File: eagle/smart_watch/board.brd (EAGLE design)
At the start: 100 x 80 mm, 38 parts, among them U1 MCP73831, U2 TPS61200, U3 MAX1704X, U4 V_REG_LDOSMD

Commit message: V1 of Schema is donepending feedback
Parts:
- removed QG1: SM77H, crystal:SM77H
- removed VIBE: (no value), SparkFun-Connectors:JST-2-PTH-NS
- added LED1, LED2, LED3, LED4: (no value), SparkFun-LED:LED-0603
- added R12, R13, R19, R20: Pullup, SparkFun-Passives:0402-RES
- added R14, R16, R17, R18: 330, SparkFun-Passives:0402-RES
- added R15: 10k, SparkFun-Passives:0402-RES
- added S1: (no value), SparkFun-Electromechanical:JOYSTICK_MINI
- added U$3: MOTOR10MM, SparkFun-Electromechanical:VIBE-MOTOR-10MM
- added Y1: (no value), SparkFun-FreqCtrl:CRYSTAL-SMD-5X3
- C1, C2: value (none) -> 4.7uF
- C12, C13: value 0.1uF -> 16pF; device SparkFun-Capacitors:0402-CAP -> SparkFun-Passives:0402-CAP
- C3, C6: value (none) -> .1uF
- C4: value (none) -> 10uF
- C5: value (none) -> 22uF
- C7: value (none) -> 1uF
- C8: value (none) -> 10nF
- L1: value (none) -> 4.7uH
- R11: value (none) -> 4.7k
- R2, R5, R6: value (none) -> 10k
- R3, R8: value (none) -> 2M
- R4: value (none) -> 100
- R7, R9: value (none) -> 220k
- U$2: value BLUERADIO_BR-C40NINTERNAL -> BLUETOOTH-RN41"; device SparkFun-RF:BLUETOOTH-INTERNAL-FP -> SparkFun-RF:RN41
- moved C13 67.1 mm to (-48.3, -16.5)
- moved C12 66.0 mm to (-48.3, -14.0)
- moved U$2 57.9 mm to (-34.3, -25.4)
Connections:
- new net ACC_INT1: ACCELEROMETER.8, U$1.10
- new net ACC_INT2: ACCELEROMETER.9, U$1.14
- new net JCENTER: S1.CTR, U$1.21
- new net JDOWN: S1.D, U$1.43
- new net JLEFT: S1.C, U$1.48
- new net JRIGHT: S1.B, U$1.18
- new net JUP: S1.A, U$1.37
- new net MISO1: U$1.26, U$2.24
- new net MOSI1: U$1.38, U$2.2
- new net N$12: LED1.A, U$2.21
- new net N$13: LED1.C, R14.2
- new net N$14: LED2.C, R16.2
- new net N$15: LED3.A, U$1.25
- new net N$16: LED4.A, U$1.24
- new net N$17: LED3.C, R17.2
- new net N$18: LED4.C, R18.2
- new net SCK1: U$1.13, U$2.6
- new net SCL: ACCELEROMETER.14, R13.1, R19.1, R20.1, U$1.15, U3.7
- new net SDA: ACCELEROMETER.13, R12.1, U$1.16, U3.8
- new net SSEL1: U$1.2, U$2.23
- new net XTALIN: C13.2, U$1.6, Y1.3
- new net XTALOUT: C12.2, U$1.7, Y1.1
- net 3.3V: now also ACCELEROMETER.7, R12.2, R13.2, R19.2, R20.2, U$2.11
- net GND: now also ACCELEROMETER.12, C12.1, C13.1, R14.1, R15.1, R16.1, R17.1, R18.1, S1.GND, U$3.-; no longer C12.2, C13.2, QG1.2, VIBE.1
- net N$1: now also LED2.A, U$2.19; no longer C13.1, QG1.3, U$1.7
- net N$11: now also R15.2, U$2.22; no longer C12.1, QG1.4, U$1.6
- net SCRX: now also U$1.46
- net SCTX: now also U$1.47
- net VIBE_PWM: now also U$1.20, U$3.+; no longer VIBE.2

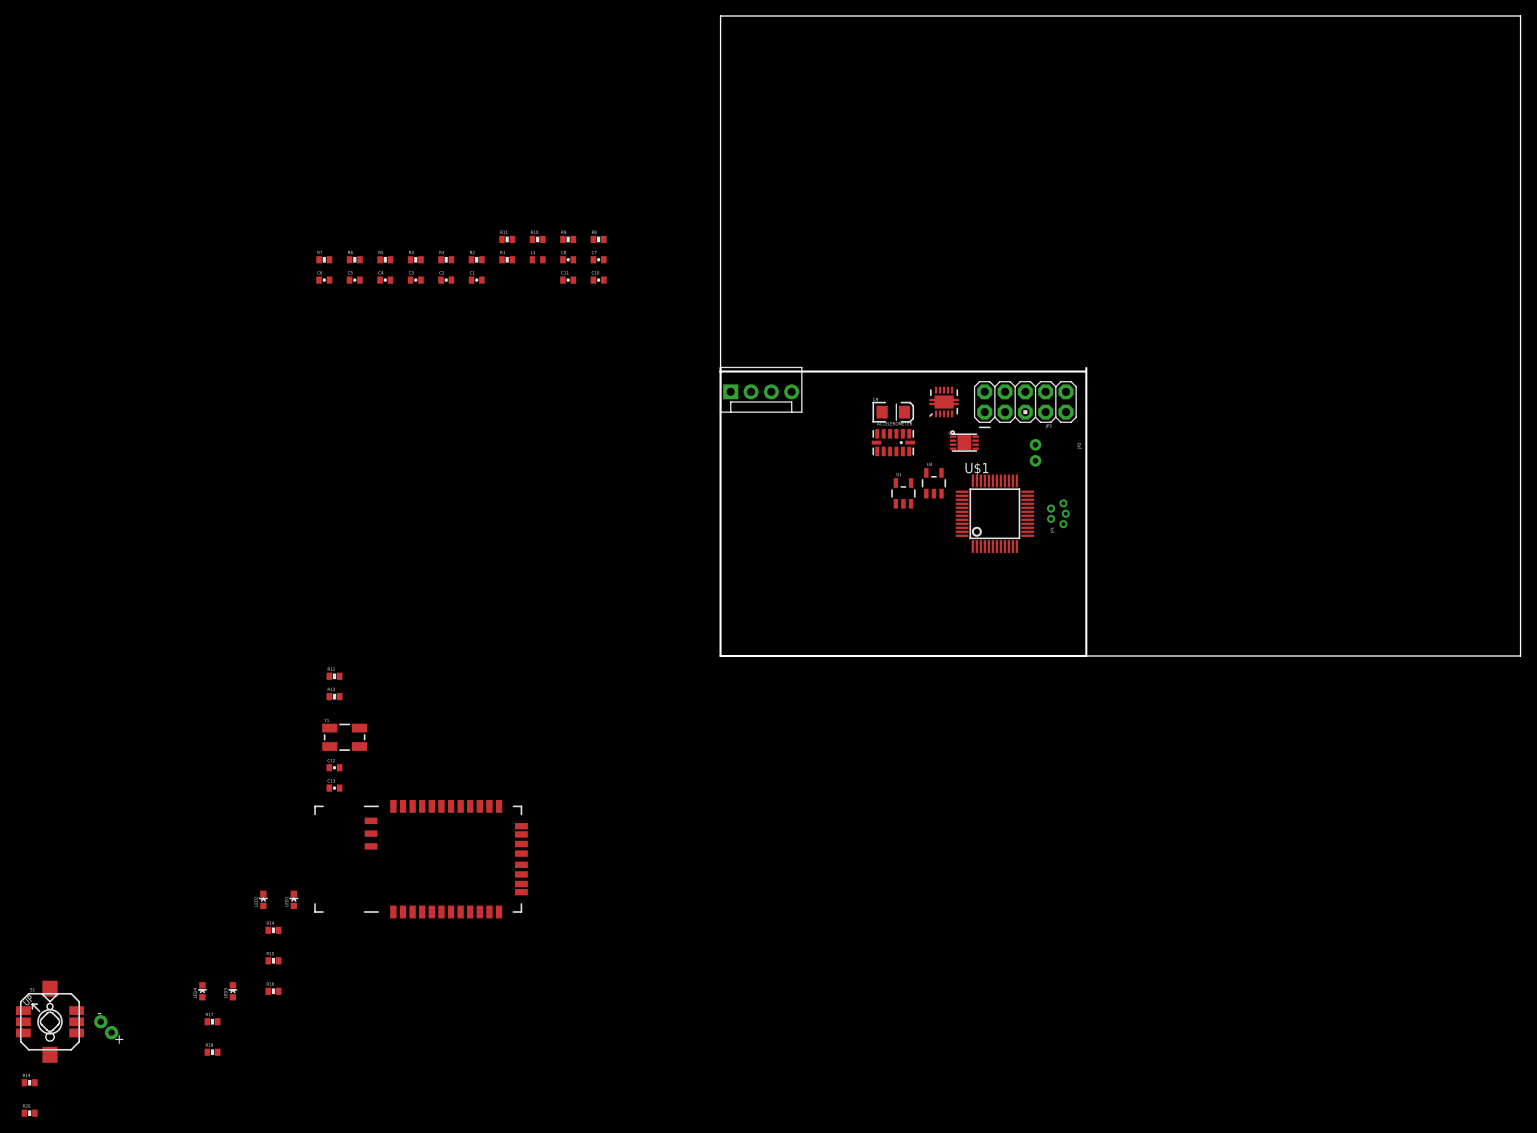
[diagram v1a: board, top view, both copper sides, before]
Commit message: Started layout Fixed up joystick wiring
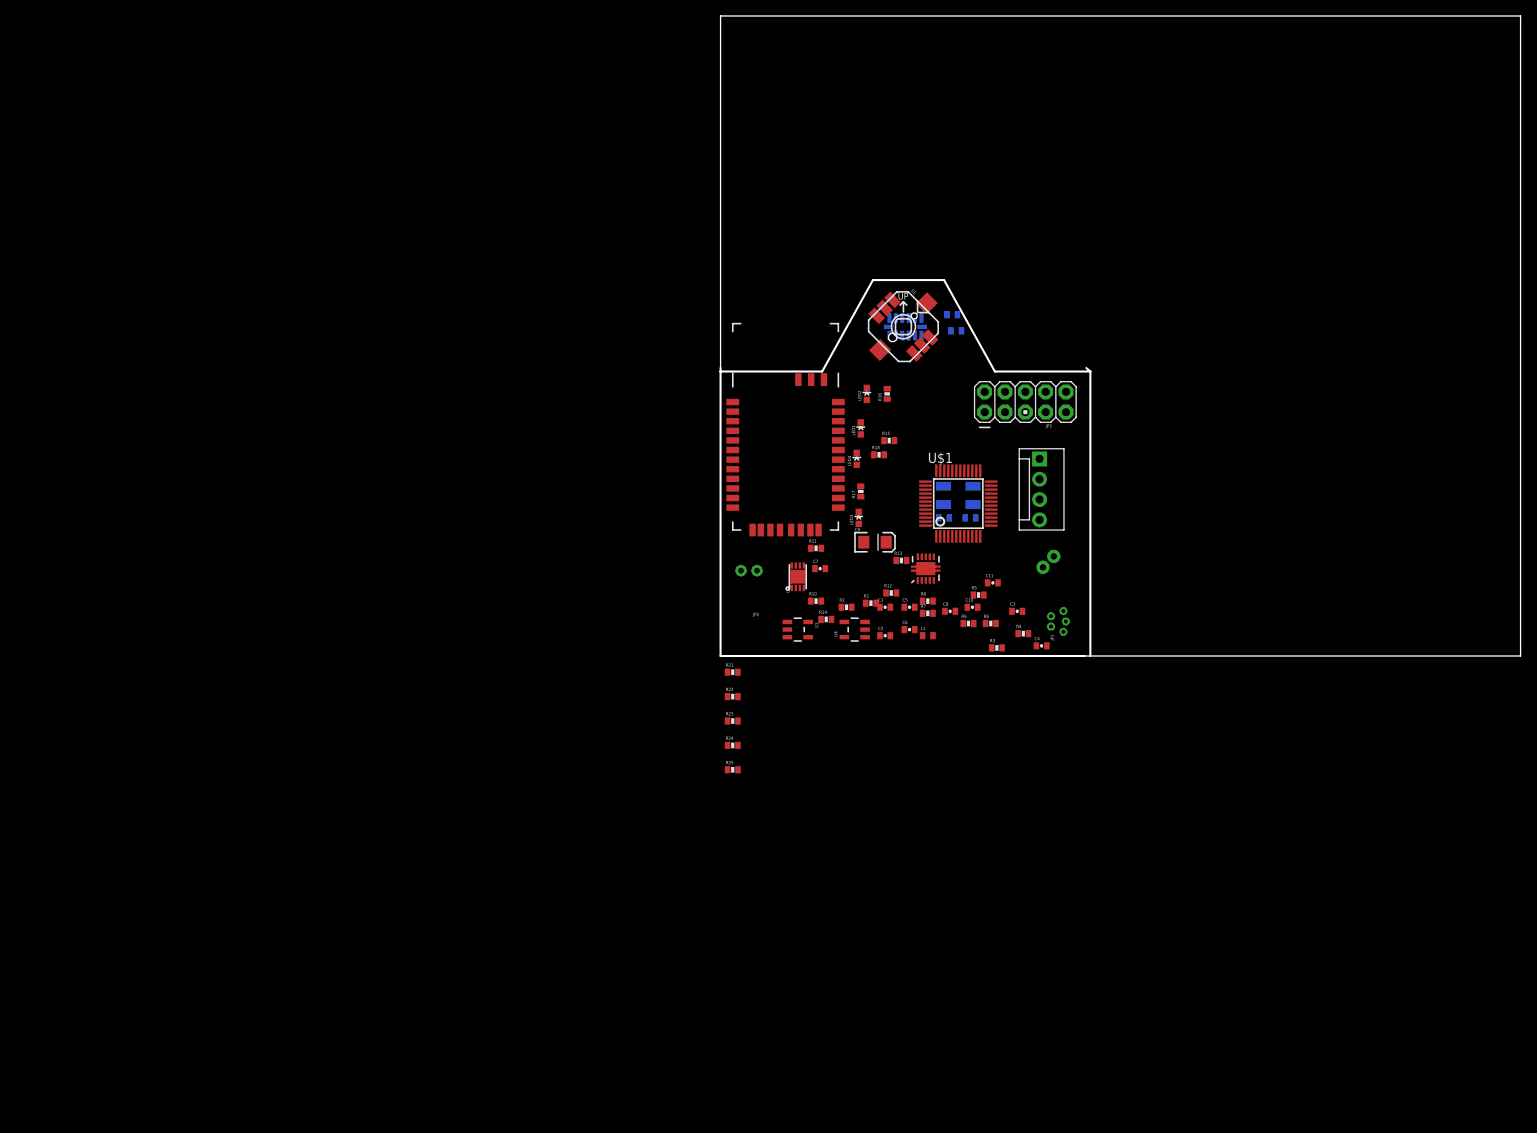
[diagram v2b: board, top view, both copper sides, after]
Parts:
- added R21, R22, R23, R24, R25: 10k, SparkFun-Passives:0402-RES
- R10: value (none) -> 1k
- Y1: value (none) -> 16MHz
- moved R20 152.5 mm to (29.0, 42.7), flipped to the bottom
- moved R19 149.2 mm to (29.5, 40.6), flipped to the bottom
- moved S1 137.6 mm to (22.9, 41.2), turned to 315 degrees
- moved U$3 121.3 mm to (35.3, 15.0), flipped to the bottom
- moved R18 111.9 mm to (19.8, 25.1)
- moved R16 107.1 mm to (20.8, 32.8), turned to 90 degrees
- moved LED4 105.4 mm to (17.0, 24.6)
- moved R17 104.7 mm to (17.5, 20.6), turned to 90 degrees
- moved R15 100.8 mm to (21.1, 26.9)
- moved LED2 98.4 mm to (18.3, 32.8)
- moved LED3 98.1 mm to (17.3, 17.3)
- moved C4 93.9 mm to (40.1, 1.27)
- moved LED1 92.2 mm to (17.5, 28.4)
- moved R6 91.6 mm to (33.8, 4.06)
- moved R4 89.2 mm to (37.8, 2.79)
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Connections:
- removed net VSS1: U$1.41
- removed net VSS2: U$1.5
- net 3.3V: now also R21.2, R22.2, R23.2, R24.2, R25.2
- net GND: now also U$1.41, U$1.5
- net JCENTER: now also R25.1, U$1.36; no longer U$1.21
- net JDOWN: now also R21.1, U$1.33; no longer U$1.43
- net JLEFT: now also R23.1, U$1.34; no longer U$1.48
- net JRIGHT: now also R24.1, U$1.35; no longer U$1.18
- net JUP: now also R22.1, U$1.31; no longer U$1.37
- net SCL: no longer R19.1
- net SDA: now also R19.1
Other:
- outline, holes or cut-outs redrawn

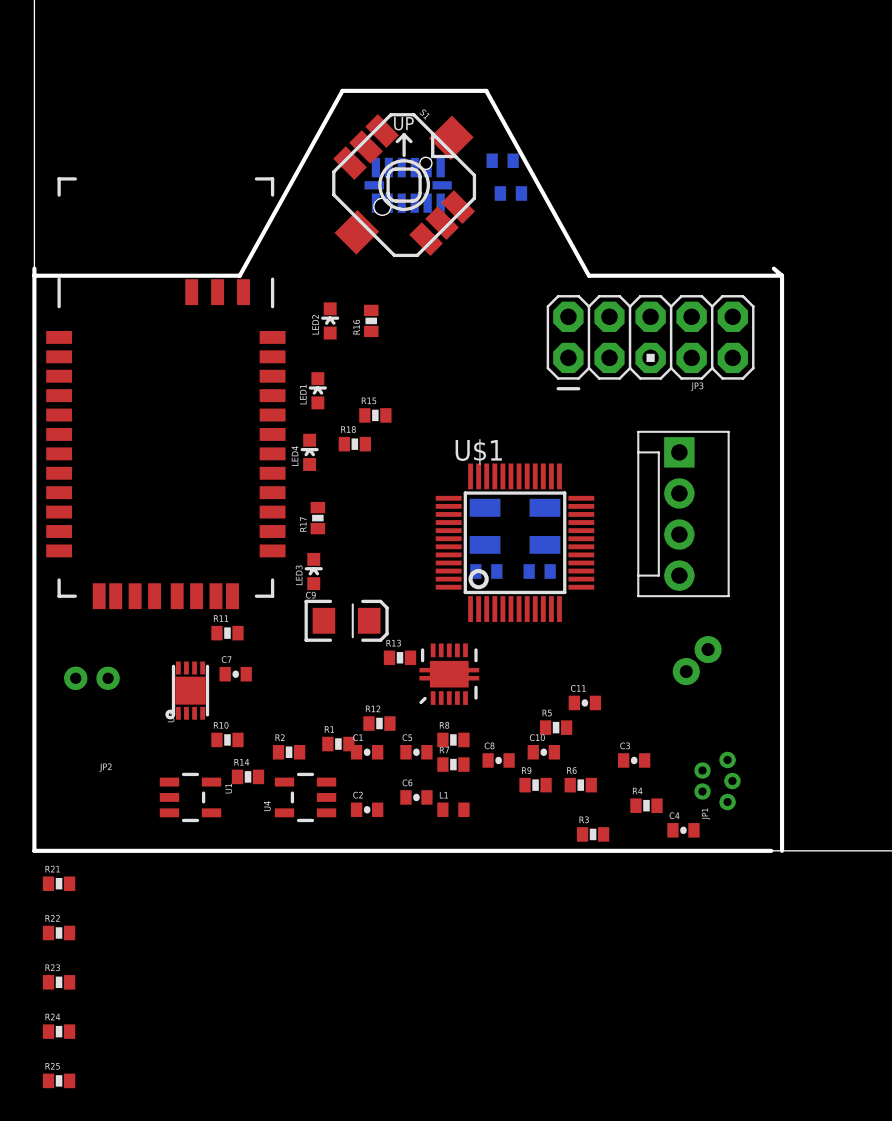
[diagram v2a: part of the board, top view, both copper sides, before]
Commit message: Finished V1 of board layout
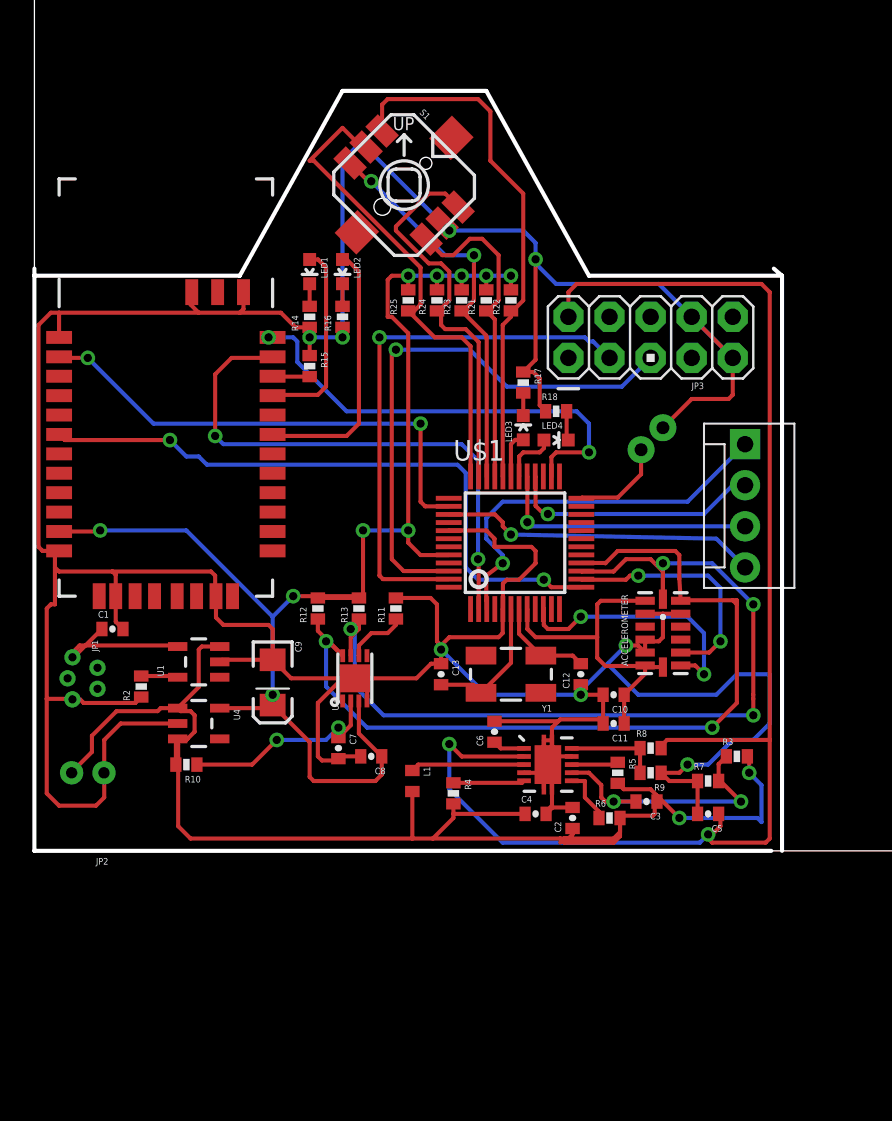
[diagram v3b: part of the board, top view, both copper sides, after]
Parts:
- removed R1: (no value), SparkFun-Passives:0402-RES
- removed R19, R20: Pullup, SparkFun-Passives:0402-RES
- moved R25 52.9 mm to (23.1, 34.0), turned to 90 degrees
- moved R24 50.9 mm to (24.9, 34.0), turned to 90 degrees
- moved R23 49.0 mm to (26.4, 34.0), turned to 90 degrees
- moved R22 48.1 mm to (29.5, 34.0), turned to 90 degrees
- moved R21 44.7 mm to (27.9, 34.0), turned to 90 degrees
- moved JP1 39.1 mm to (3.30, 10.7), turned to 270 degrees
- moved ACCELEROMETER 31.9 mm to (38.9, 13.5), flipped to the top, turned to 90 degrees
- moved R14 28.7 mm to (17.0, 33.0), turned to 90 degrees
- moved C5 18.4 mm to (41.7, 2.29), turned to 180 degrees
- moved C1 17.5 mm to (4.83, 13.7)
- moved R7 15.8 mm to (41.7, 4.32)
- moved LED3 15.7 mm to (30.2, 26.2)
- moved LED4 15.3 mm to (32.3, 25.4), turned to 270 degrees
- moved R17 15.2 mm to (30.2, 29.0), turned to 270 degrees
- moved U$3 14.0 mm to (32.5, 28.7)
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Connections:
- new net VBUS: C1.1, JP1.1, U1.4
- net 3.3V: no longer R19.2, R20.2
- net GND: no longer R1.1
- net JUP: now also U$1.32; no longer U$1.31
- net N$15: now also U$1.31; no longer U$1.25
- net N$16: now also U$1.30; no longer U$1.24
- net N$2: no longer R1.2
- net SCL: no longer R20.1
- net SDA: no longer R19.1
- net VBATT: now also R10.2; no longer C1.1, JP1.1, U1.4
- net VIBE_PWM: now also U$1.24; no longer U$1.20
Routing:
- net GND: track 0.00 -> 282.0 mm, vias 0 -> 8
- net 3.3V: track 0.00 -> 107.6 mm, vias 0 -> 10
- net VBATT: track 0.00 -> 88.9 mm, vias 0 -> 2
- net 5V: track 0.00 -> 86.6 mm, vias 0 -> 2
- net SCL: track 0.00 -> 55.5 mm, vias 0 -> 4
- net SDA: track 0.00 -> 53.7 mm, vias 0 -> 2
- net SCK1: track 0.00 -> 39.6 mm, vias 0 -> 2
- net SCRX: track 0.00 -> 34.3 mm, vias 0 -> 1
- net SSEL1: track 0.00 -> 33.9 mm, vias 0 -> 2
- net SCTX: track 0.00 -> 33.9 mm, vias 0 -> 1
- net JUP: track 0.00 -> 32.8 mm
- net MOSI1: track 0.00 -> 30.7 mm, vias 0 -> 2
- net JCENTER: track 0.00 -> 30.4 mm
- net MISO1: track 0.00 -> 28.4 mm, vias 0 -> 2
- net JLEFT: track 0.00 -> 24.7 mm, vias 0 -> 2
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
